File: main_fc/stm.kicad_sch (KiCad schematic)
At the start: 47 parts, among them J4 Conn_02x07_Odd_Even, J6 SD_Card_Receptacle, U4 STM32H730ZBTx, U5 REF4132B25DBVR

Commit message: main flight computer annotations and passive footprints
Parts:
- C15, C16, C17, C18, C19, C20, C21, C22, C23, C24, C25, C26: footprint (none) -> Capacitor_SMD:C_0603_1608Metric
- C27, C29, C30, C31, C32, C33, C34, C35, C36, C37, C38, C39, C40: renamed from C?; footprint (none) -> Capacitor_SMD:C_0603_1608Metric
- C28: renamed from C27; footprint (none) -> Capacitor_SMD:C_0603_1608Metric
- R15, R16, R17, R18, R19, R20, R21, R22, R23, R24, R25: footprint (none) -> Resistor_SMD:R_0603_1608Metric
- gave numbers to parts that had none: 6
- renumbered J6 to J5

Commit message: updated library
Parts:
- CR2: footprint ST485BDR:SO-8_STM -> avi_footprint:SO-8_STM-M

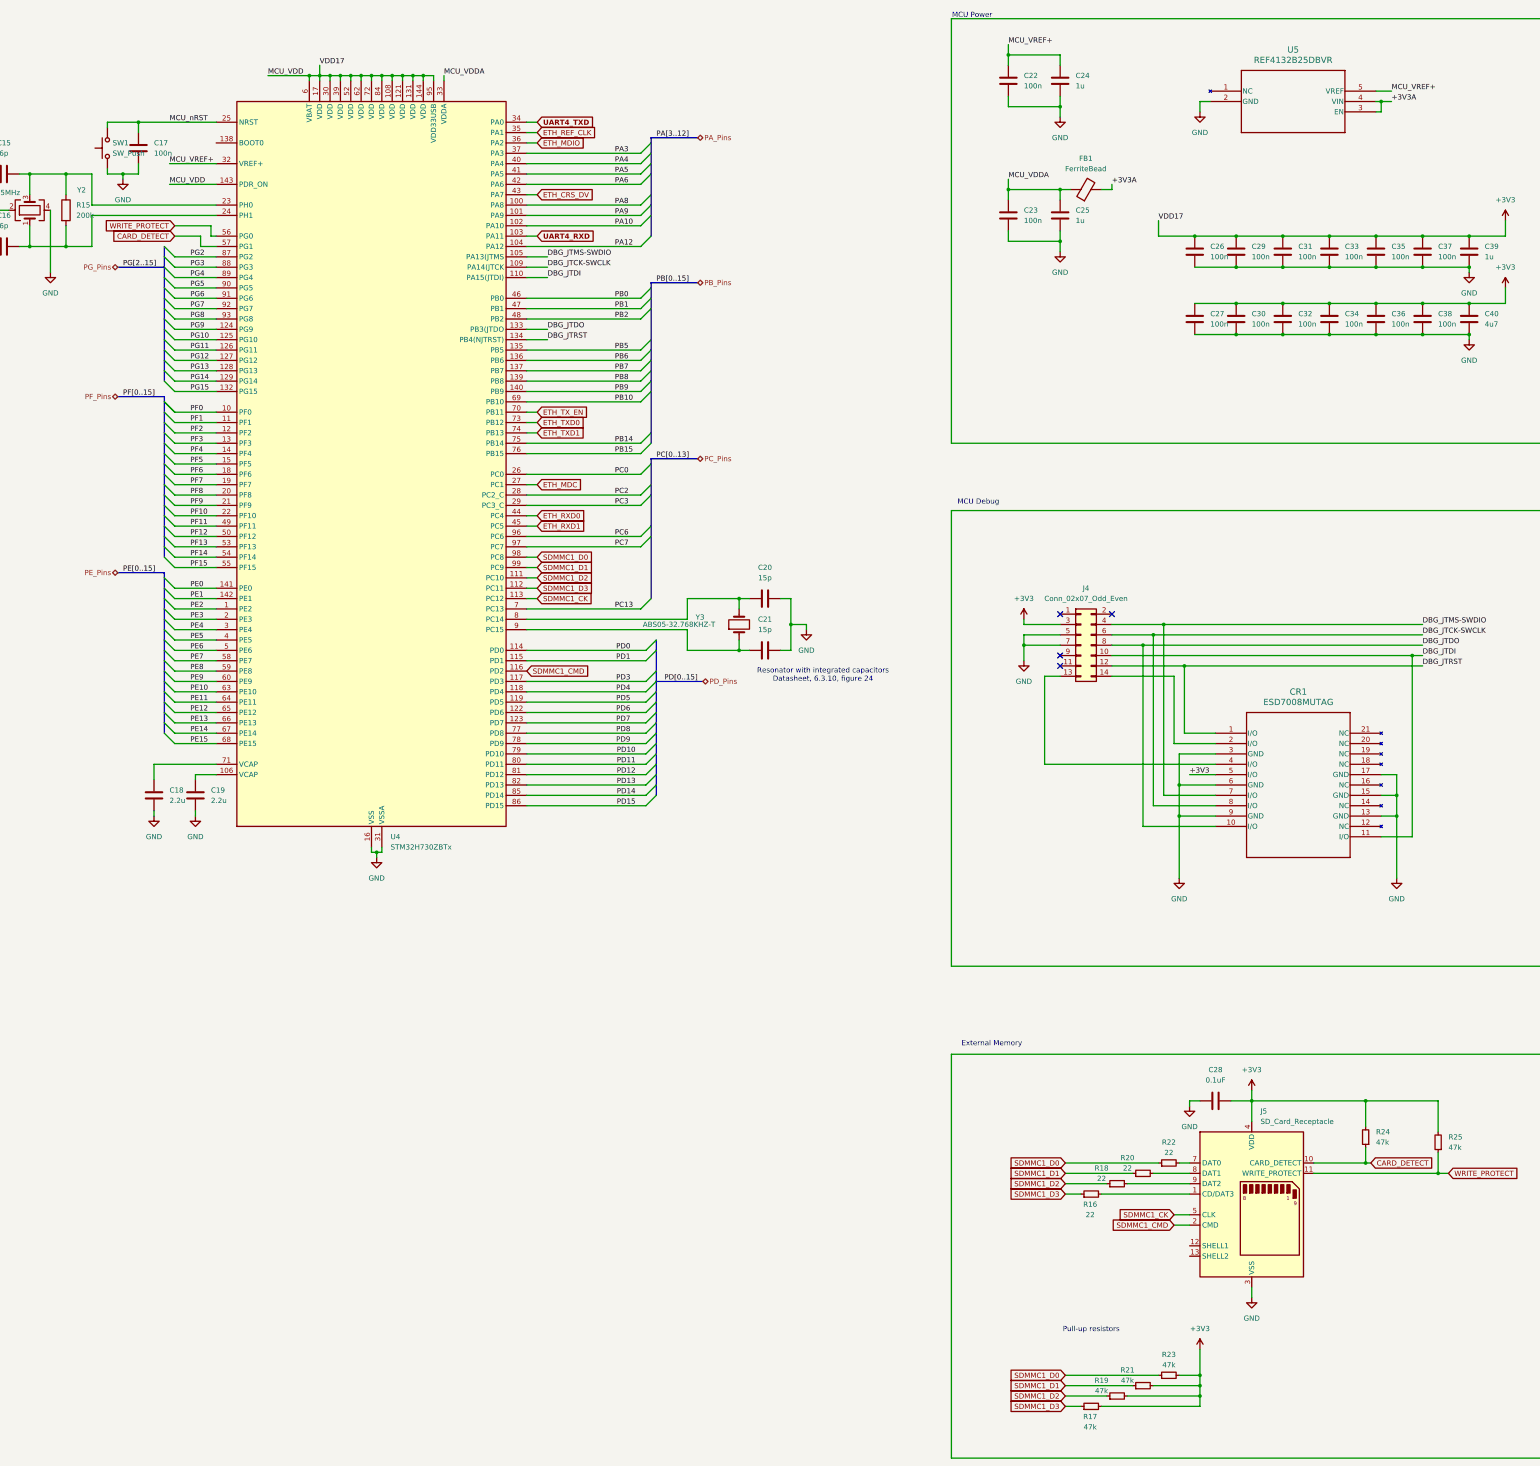
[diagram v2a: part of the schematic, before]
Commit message: added new stm symbol/footprint
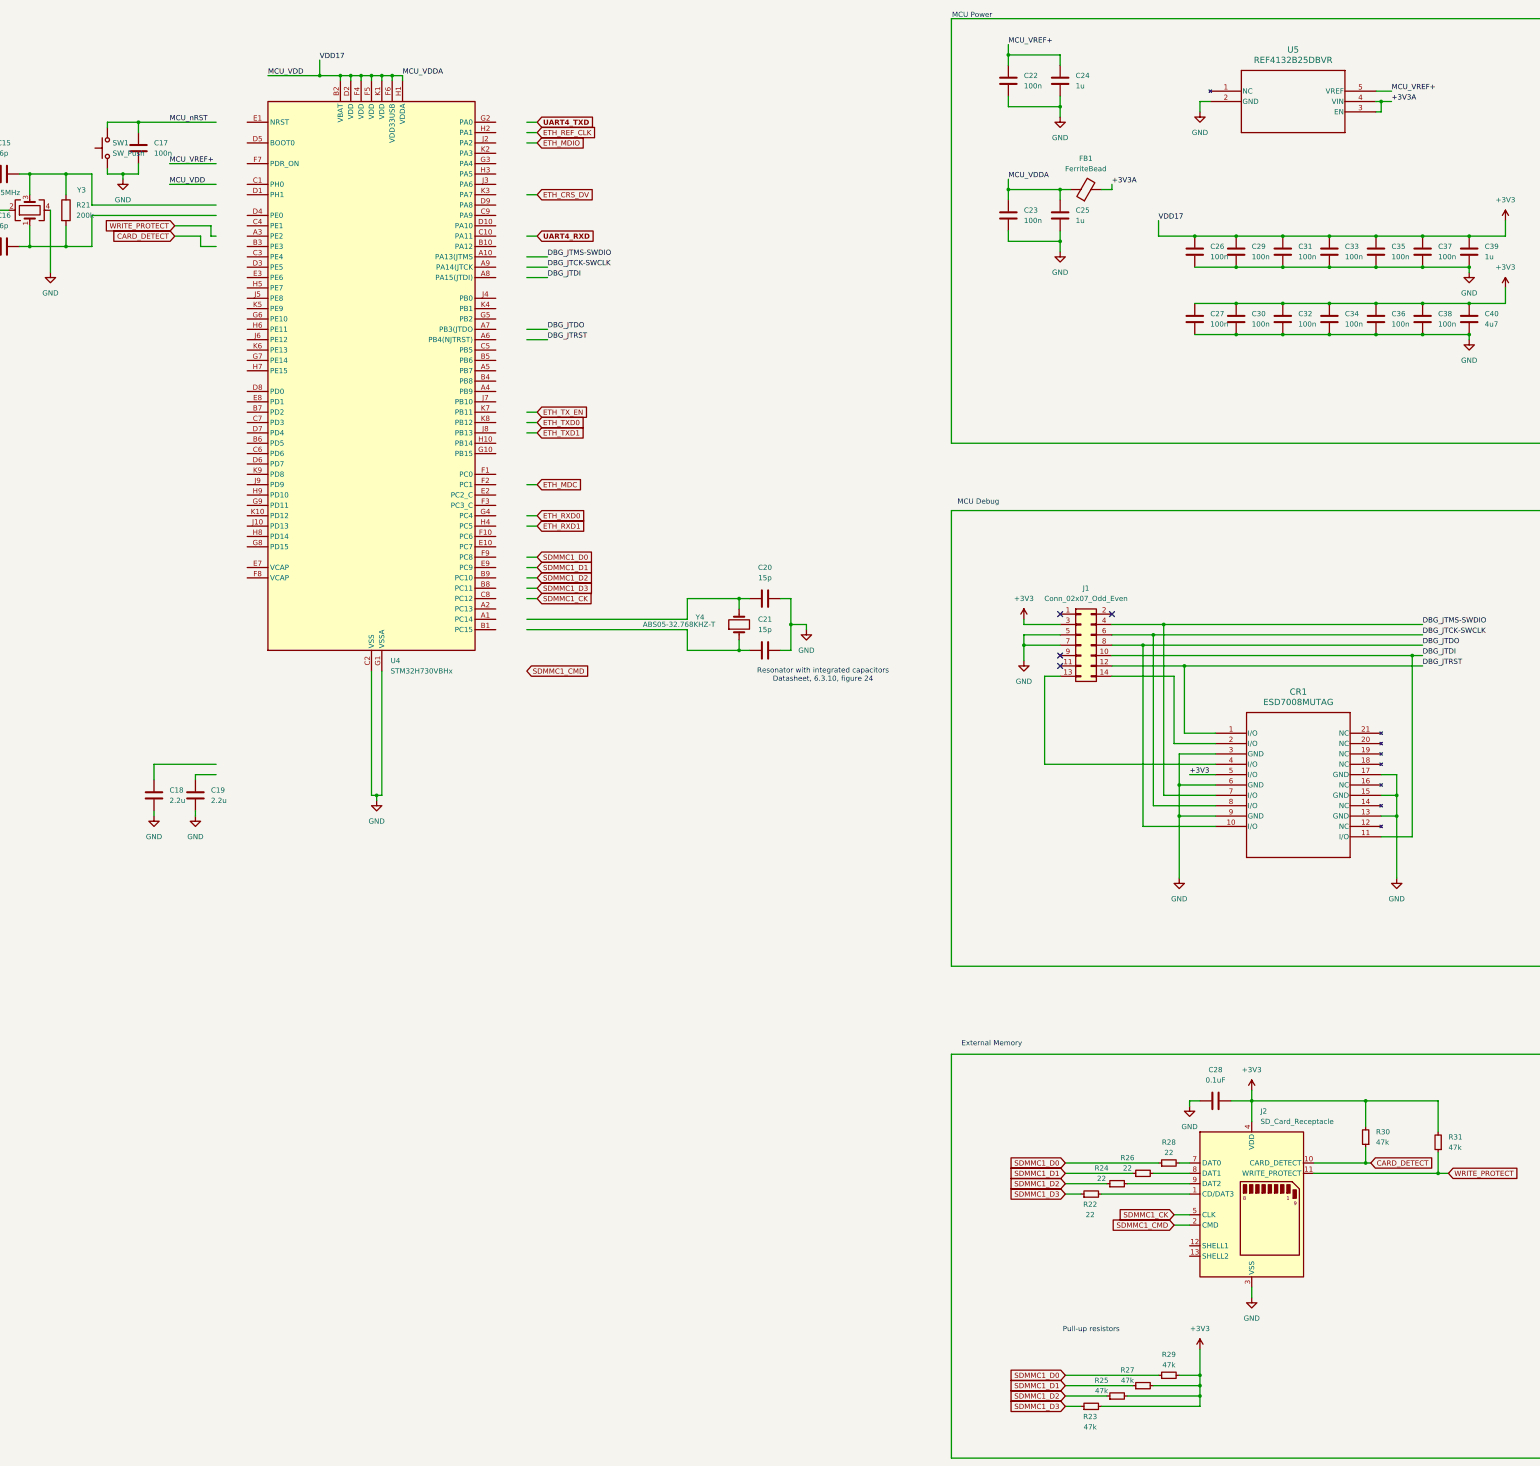
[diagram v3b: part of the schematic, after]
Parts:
- removed U4: STM32H730ZBTx, Package_QFP:LQFP-144_20x20mm_P0.5mm, symbol MCU_ST_STM32H7:STM32H730ZBTx
- added U4: STM32H730VBHx, Package_BGA:TFBGA-100_8x8mm_Layout10x10_P0.8mm, symbol MCU_ST_STM32H7:STM32H730VBHx
- renumbered J4 to J1, J5 to J2, R15 to R21, R16 to R22, R17 to R23, R18 to R24, R19 to R25, R20 to R26, R21 to R27, R22 to R28, R23 to R29, R24 to R30, R25 to R31, Y2 to Y3, Y3 to Y4
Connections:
- net MCU_VDDA is gone; now on net +3V3: C23.1, C25.1, FB1.1
- net +3V3: now also U4.B2 (VBAT), U4.D2 (VDD), U4.F4 (VDD), U4.F5 (VDD), U4.F6 (VDD33USB), U4.H1 (VDDA), U4.K1 (VDD)
- net GND: now also U4.C2 (VSS), U4.E4 (VSS), U4.E5 (VSS), U4.E6 (VSS), U4.G1 (VSSA), U4.J1 (VSS)

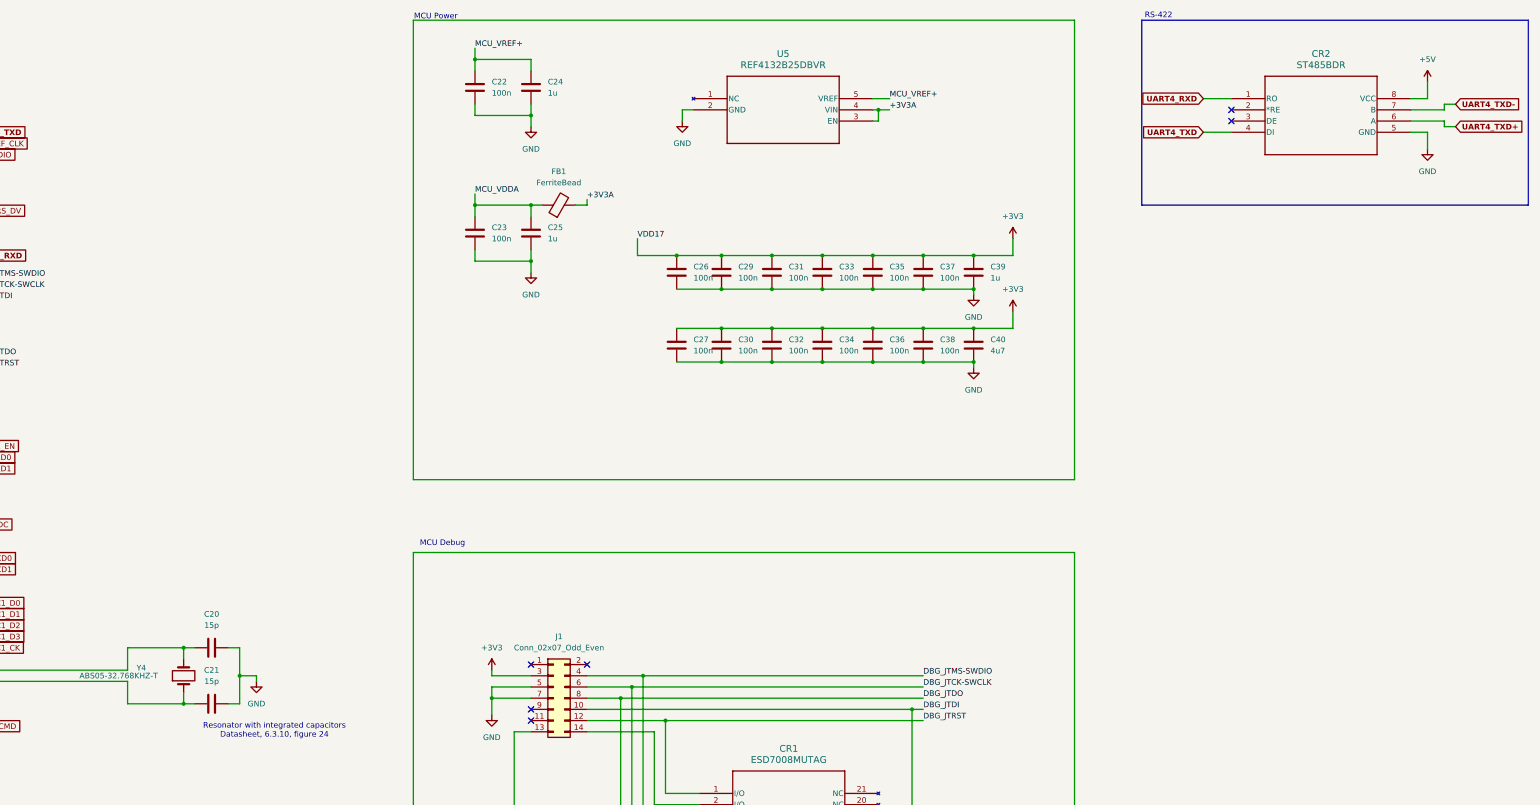
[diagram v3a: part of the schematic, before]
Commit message: Added footprints for stm sheet to lib folder
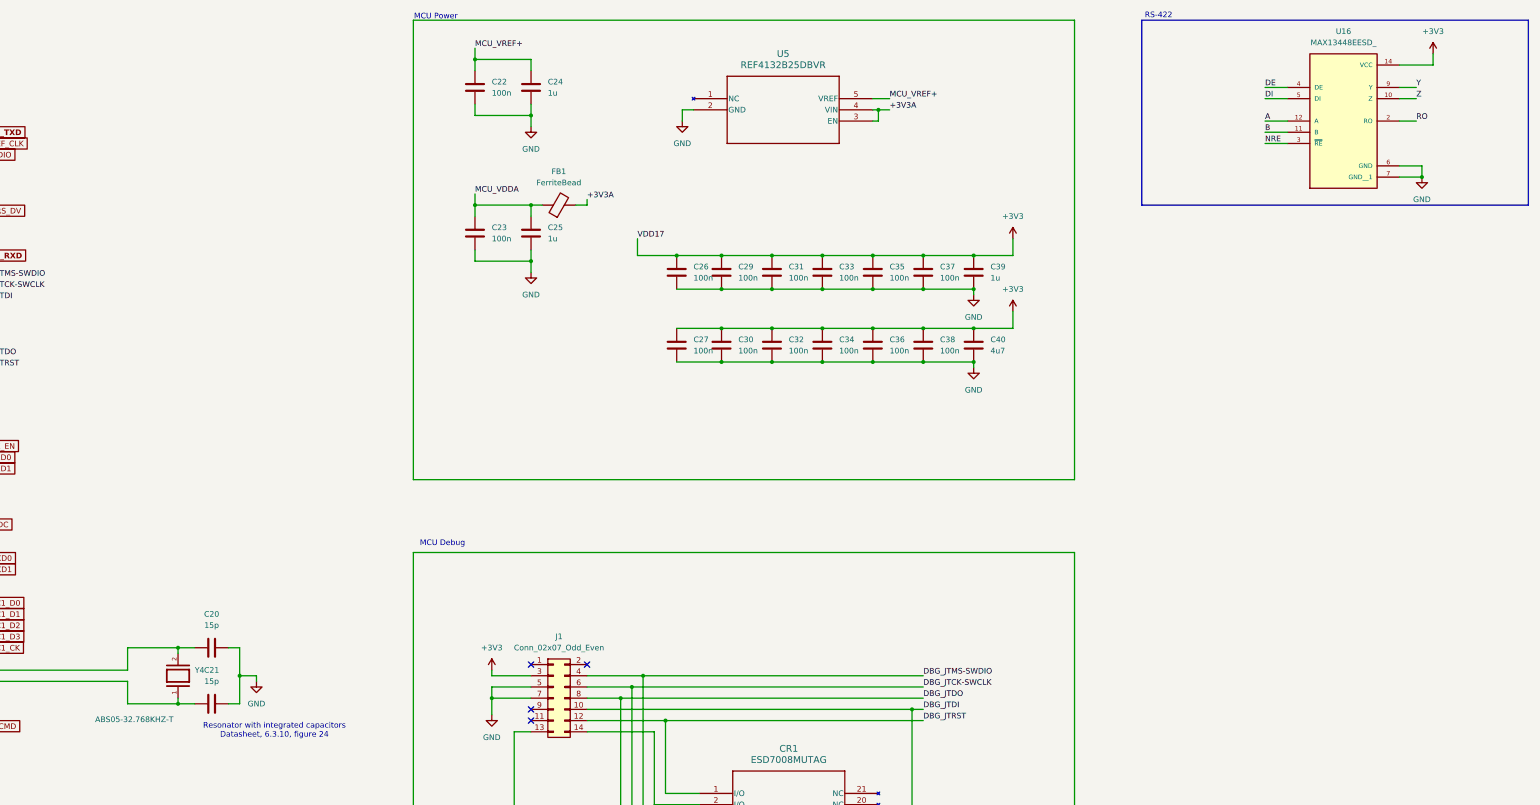
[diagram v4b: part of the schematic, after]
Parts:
- removed CR2: ST485BDR, avi_footprint:SO-8_STM-M, symbol 2025-09-03_13-52-52:ST485BDR
- removed Y4: ABS05-32.768KHZ-T, symbol Device:Crystal
- added U16: MAX13448EESD_, avi_footprint:SOIC127P600X175-14N, symbol MAX13448EESD:MAX13448EESD_
- added Y4: ABS05-32.768KHZ-T, avi_footprint:XTAL_ABS05-32.768KHZ-T, symbol ABS05-32.768KHZ-T:ABS05-32.768KHZ-T
- CR1: footprint (none) -> avi_footprint:UDFN18_517BV_ONS
- U5: footprint (none) -> avi_footprint:SOT-23-5_DBV_TEX
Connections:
- net +3V3: now also U16.14 (VCC)
- net GND: now also U16.6 (GND), U16.7 (GND__1)
- net at C21.1: now also Y4.1
- net at C20.1: now also Y4.2
- new net A: U16.12 (A)
- new net B: U16.11 (B)
- new net DE: U16.4 (DE)
- new net DI: U16.5 (DI)
- new net NRE: U16.3 (~{RE})
- new net RO: U16.2 (RO)
- new net Y: U16.9 (Y)
- new net Z: U16.10 (Z)
- no-connect marks 6 -> 4
